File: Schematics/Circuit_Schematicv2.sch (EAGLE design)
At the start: 66 parts, among them Q2 LE33CZ

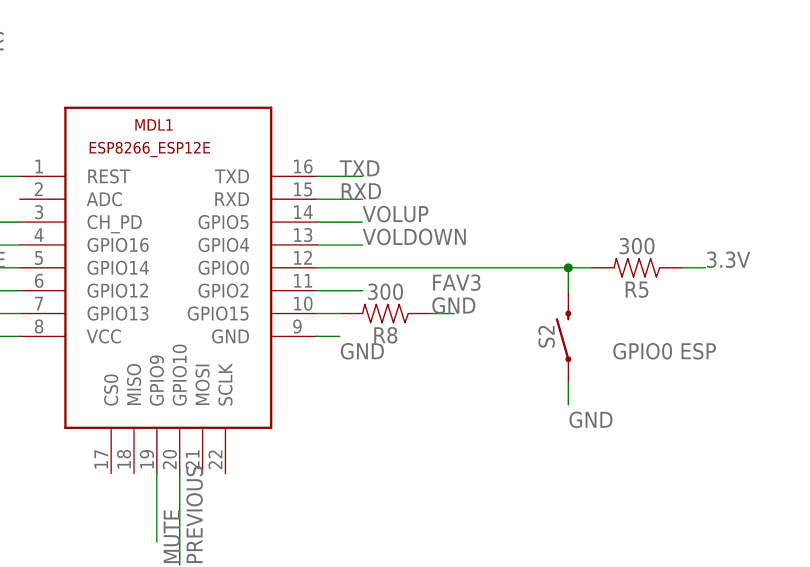
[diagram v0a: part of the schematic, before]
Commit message: Finished the PCB board and schematic
Changes might have to be made based on the testing on Friday the 10th
March
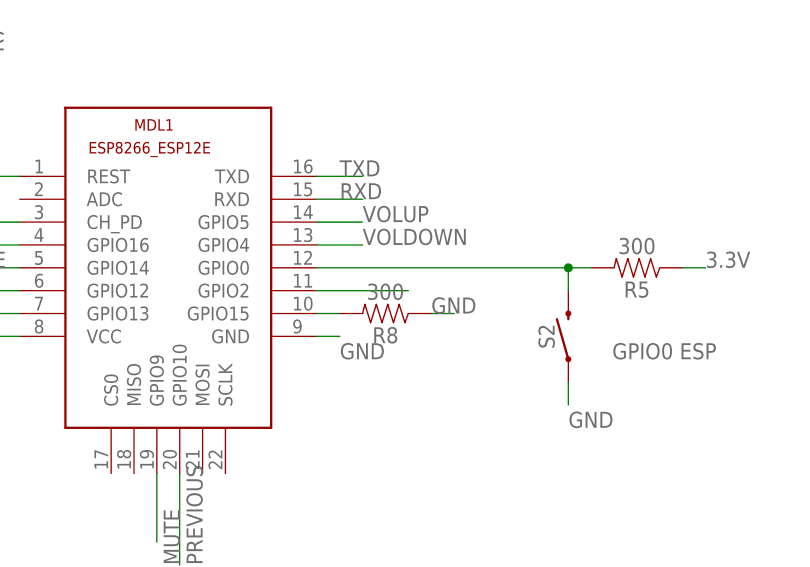
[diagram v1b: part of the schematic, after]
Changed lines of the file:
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@@
 <?xml version="1.0" encoding="utf-8"?>
 <!DOCTYPE eagle SYSTEM "eagle.dtd">
-<eagle version="8.0.0">
+<eagle version="8.0.2">
 <drawing>
 <settings>
@@
 <segment>
 <pinref part="MDL1" gate="G$1" pin="GPIO2"/>
-<wire x1="403.86" y1="50.8" x2="408.94" y2="50.8" width="0.1524" layer="91"/>
-<label x="416.56" y="50.8" size="1.778" layer="95"/>
-</segment>
-</net>
+<wire x1="403.86" y1="50.8" x2="414.02" y2="50.8" width="0.1524" layer="91"/>
+</segment>
+</net>

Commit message: finished the PCB
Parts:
- D1: value (none) -> BLUE; device adafruit:LED -> SparkFun-LED:LED-BLUE1206
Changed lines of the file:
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@@
 <grid distance="0.1" unitdist="inch" unit="inch" style="lines" multiple="1" display="no" altdistance="0.01" altunitdist="inch" altunit="inch"/>
 <layers>
-<layer number="1" name="Top" color="4" fill="1" visible="no" active="no"/>
-<layer number="2" name="Route2" color="1" fill="3" visible="no" active="no"/>
-<layer number="3" name="Route3" color="4" fill="3" visible="no" active="no"/>
-<layer number="4" name="Route4" color="1" fill="4" visible="no" active="no"/>
-<layer number="5" name="Route5" color="4" fill="4" visible="no" active="no"/>
-<layer number="6" name="Route6" color="1" fill="8" visible="no" active="no"/>
-<layer number="7" name="Route7" color="4" fill="8" visible="no" active="no"/>
-<layer number="8" name="Route8" color="1" fill="2" visible="no" active="no"/>
-<layer number="9" name="Route9" color="4" fill="2" visible="no" active="no"/>
-<layer number="10" name="Route10" color="1" fill="7" visible="no" active="no"/>
-<layer number="11" name="Route11" color="4" fill="7" visible="no" active="no"/>
-<layer number="12" name="Route12" color="1" fill="5" visible="no" active="no"/>
-<layer number="13" name="Route13" color="4" fill="5" visible="no" active="no"/>
-<layer number="14" name="Route14" color="1" fill="6" visible="no" active="no"/>
-<layer number="15" name="Route15" color="4" fill="6" visible="no" active="no"/>
-<layer number="16" name="Bottom" color="1" fill="1" visible="no" active="no"/>
-<layer number="17" name="Pads" color="2" fill="1" visible="no" active="no"/>
-<layer number="18" name="Vias" color="2" fill="1" visible="no" active="no"/>
-<layer number="19" name="Unrouted" color="6" fill="1" visible="no" active="no"/>
-<layer number="20" name="Dimension" color="15" fill="1" visible="no" active="no"/>
-<layer number="21" name="tPlace" color="7" fill="1" visible="no" active="no"/>
-<layer number="22" name="bPlace" color="7" fill="1" visible="no" active="no"/>
-<layer number="23" name="tOrigins" color="15" fill="1" visible="no" active="no"/>
-<layer number="24" name="bOrigins" color="15" fill="1" visible="no" active="no"/>
-<layer number="25" name="tNames" color="7" fill="1" visible="no" active="no"/>
-<layer number="26" name="bNames" color="7" fill="1" visible="no" active="no"/>
-<layer number="27" name="tValues" color="7" fill="1" visible="no" active="no"/>
-<layer number="28" name="bValues" color="7" fill="1" visible="no" active="no"/>
+<layer number="1" name="Top" color="4" fill="1" visible="yes" active="no"/>
+<layer number="2" name="Route2" color="1" fill="3" visible="yes" active="no"/>
+<layer number="3" name="Route3" color="4" fill="3" visible="yes" active="no"/>
+<layer number="4" name="Route4" color="1" fill="4" visible="yes" active="no"/>
+<layer number="5" name="Route5" color="4" fill="4" visible="yes" active="no"/>
+<layer number="6" name="Route6" color="1" fill="8" visible="yes" active="no"/>
+<layer number="7" name="Route7" color="4" fill="8" visible="yes" active="no"/>
+<layer number="8" name="Route8" color="1" fill="2" visible="yes" active="no"/>
+<layer number="9" name="Route9" color="4" fill="2" visible="yes" active="no"/>
+<layer number="10" name="Route10" color="1" fill="7" visible="yes" active="no"/>
+<layer number="11" name="Route11" color="4" fill="7" visible="yes" active="no"/>
+<layer number="12" name="Route12" color="1" fill="5" visible="yes" active="no"/>
+<layer number="13" name="Route13" color="4" fill="5" visible="yes" active="no"/>
+<layer number="14" name="Route14" color="1" fill="6" visible="yes" active="no"/>
+<layer number="15" name="Route15" color="4" fill="6" visible="yes" active="no"/>
+<layer number="16" name="Bottom" color="1" fill="1" visible="yes" active="no"/>
+<layer number="17" name="Pads" color="2" fill="1" visible="yes" active="no"/>
+<layer number="18" name="Vias" color="2" fill="1" visible="yes" active="no"/>
+<layer number="19" name="Unrouted" color="6" fill="1" visible="yes" active="no"/>
+<layer number="20" name="Dimension" color="15" fill="1" visible="yes" active="no"/>
+<layer number="21" name="tPlace" color="7" fill="1" visible="yes" active="no"/>
+<layer number="22" name="bPlace" color="7" fill="1" visible="yes" active="no"/>
+<layer number="23" name="tOrigins" color="15" fill="1" visible="yes" active="no"/>
+<layer number="24" name="bOrigins" color="15" fill="1" visible="yes" active="no"/>
+<layer number="25" name="tNames" color="7" fill="1" visible="yes" active="no"/>
+<layer number="26" name="bNames" color="7" fill="1" visible="yes" active="no"/>
+<layer number="27" name="tValues" color="7" fill="1" visible="yes" active="no"/>
+<layer number="28" name="bValues" color="7" fill="1" visible="yes" active="no"/>
 <layer number="29" name="tStop" color="7" fill="3" visible="no" active="no"/>
 <layer number="30" name="bStop" color="7" fill="6" visible="no" active="no"/>
@@
 <layer number="35" name="tGlue" color="7" fill="4" visible="no" active="no"/>
 <layer number="36" name="bGlue" color="7" fill="5" visible="no" active="no"/>
-<layer number="37" name="tTest" color="7" fill="1" visible="no" active="no"/>
-<layer number="38" name="bTest" color="7" fill="1" visible="no" active="no"/>
+<layer number="37" name="tTest" color="7" fill="1" visible="yes" active="no"/>
+<layer number="38" name="bTest" color="7" fill="1" visible="yes" active="no"/>
 <layer number="39" name="tKeepout" color="4" fill="11" visible="no" active="no"/>
 <layer number="40" name="bKeepout" color="1" fill="11" visible="no" active="no"/>
@@
 <layer number="44" name="Drills" color="7" fill="1" visible="no" active="no"/>
 <layer number="45" name="Holes" color="7" fill="1" visible="no" active="no"/>
-<layer number="46" name="Milling" color="3" fill="1" visible="no" active="no"/>
-<layer number="47" name="Measures" color="7" fill="1" visible="no" active="no"/>
-<layer number="48" name="Document" color="7" fill="1" visible="no" active="no"/>
-<layer number="49" name="Reference" color="7" fill="1" visible="no" active="no"/>
-<layer number="50" name="dxf" color="7" fill="1" visible="no" active="no"/>
-<layer number="51" name="tDocu" color="7" fill="1" visible="no" active="no"/>
-<layer number="52" name="bDocu" color="7" fill="1" visible="no" active="no"/>
-<layer number="53" name="tGND_GNDA" color="7" fill="9" visible="no" active="no"/>
-<layer number="54" name="bGND_GNDA" color="1" fill="9" visible="no" active="no"/>
-<layer number="56" name="wert" color="7" fill="1" visible="no" active="no"/>
-<layer number="57" name="tCAD" color="7" fill="1" visible="no" active="no"/>
-<layer number="59" name="tCarbon" color="7" fill="1" visible="no" active="no"/>
-<layer number="60" name="bCarbon" color="7" fill="1" visible="no" active="no"/>
+<layer number="46" name="Milling" color="3" fill="1" visible="yes" active="no"/>
+<layer number="47" name="Measures" color="7" fill="1" visible="yes" active="no"/>
+<layer number="48" name="Document" color="7" fill="1" visible="yes" active="no"/>
+<layer number="49" name="Reference" color="7" fill="1" visible="yes" active="no"/>
+<layer number="50" name="dxf" color="7" fill="1" visible="yes" active="no"/>
+<layer number="51" name="tDocu" color="7" fill="1" visible="yes" active="no"/>
+<layer number="52" name="bDocu" color="7" fill="1" visible="yes" active="no"/>
+<layer number="53" name="tGND_GNDA" color="7" fill="9" visible="yes" active="no"/>
+<layer number="54" name="bGND_GNDA" color="1" fill="9" visible="yes" active="no"/>
+<layer number="56" name="wert" color="7" fill="1" visible="yes" active="no"/>
+<layer number="57" name="tCAD" color="7" fill="1" visible="yes" active="no"/>
+<layer number="59" name="tCarbon" color="7" fill="1" visible="yes" active="no"/>
+<layer number="60" name="bCarbon" color="7" fill="1" visible="yes" active="no"/>
 <layer number="90" name="Modules" color="5" fill="1" visible="yes" active="yes"/>
 <layer number="91" name="Nets" color="2" fill="1" visible="yes" active="yes"/>
@@
 <part name="VR1" library="SparkFun-Resistors" deviceset="TRIMPOT" device="-SMD-3MM-OPEN-1/10W-25%" value="10k"/>
 <part name="MDL1" library="ESP8266-12E" deviceset="ESP8266-12E" device="ESP8266-ESP12E"/>
-<part name="D1" library="adafruit" deviceset="LED" device=""/>
+<part name="D1" library="SparkFun-LED" deviceset="LED-BLUE" device="1206" value="BLUE"/>
 <part name="R1" library="SparkFun-Resistors" deviceset="1OHM" device="-0603-1/10W-1%" value="300"/>
 <part name="U$3" library="MIRO" deviceset="24C64" device=""/>

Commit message: Final changes to make ESP work
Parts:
- added R18: 300, SparkFun-Resistors:1OHM-0603-1/10W-1%
- added S1: GPIO0 ESP, SparkFun-Switches:MOMENTARY-SWITCH-SPST-SMD-6.0X3.5MM
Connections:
- removed net N$8: MDL1.GPIO0, R5.2, S2.2
- net ENABLE: now also R18.2; no longer MDL1.GPIO14
- net GND: now also S1.1
- net MUTE: now also MDL1.GPIO14, R18.1, S1.2; no longer MDL1.GPIO9
- net PREVIOUS: now also MDL1.GPIO0, R5.2, S2.2; no longer MDL1.GPIO10

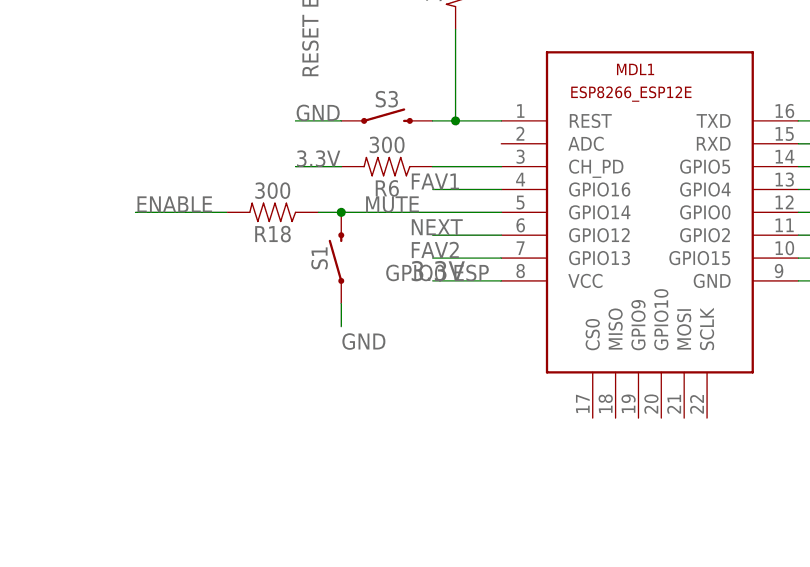
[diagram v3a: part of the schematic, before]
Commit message: Removed unnecessary switch that I put in on GPIO14
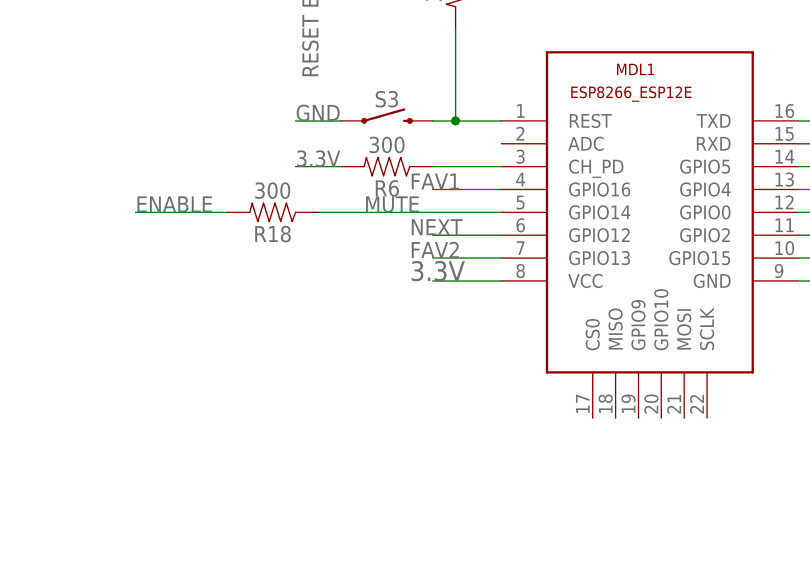
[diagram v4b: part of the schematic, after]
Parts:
- removed S1: GPIO0 ESP, SparkFun-Switches:MOMENTARY-SWITCH-SPST-SMD-6.0X3.5MM
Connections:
- net GND: no longer S1.1
- net MUTE: no longer S1.2
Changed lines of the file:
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@@
 <part name="VR5" library="SparkFun-Resistors" deviceset="TRIMPOT" device="-SMD-3MM-OPEN-1/10W-25%" value="4.7k"/>
 <part name="R18" library="SparkFun-Resistors" deviceset="1OHM" device="-0603-1/10W-1%" value="300"/>
-<part name="S1" library="SparkFun-Switches" deviceset="MOMENTARY-SWITCH-SPST" device="-SMD-6.0X3.5MM" value="GPIO0 ESP"/>
 </parts>
 <sheets>
@@
 <instance part="VR5" gate="R?" x="7.62" y="111.76"/>
 <instance part="R18" gate="G$1" x="345.44" y="53.34" rot="R180"/>
-<instance part="S1" gate="G$1" x="353.06" y="48.26" smashed="yes" rot="R90">
-<attribute name="NAME" x="351.536" y="48.26" size="1.778" layer="95" font="vector" rot="R90" align="bottom-center"/>
-<attribute name="VALUE" x="363.728" y="45.72" size="1.778" layer="96" font="vector" rot="R180" align="top-center"/>
-</instance>
 </instances>
 <busses>
@@
 <pinref part="U$2" gate="G$1" pin="GND"/>
 <wire x1="58.42" y1="101.6" x2="40.64" y2="101.6" width="0.1524" layer="91"/>
-</segment>
-<segment>
-<pinref part="S1" gate="G$1" pin="1"/>
-<wire x1="353.06" y1="43.18" x2="353.06" y2="40.64" width="0.1524" layer="91"/>
-<label x="353.06" y="38.1" size="1.778" layer="95"/>
 </segment>
 </net>
@@
 <segment>
 <pinref part="MDL1" gate="G$1" pin="GPIO14"/>
-<pinref part="S1" gate="G$1" pin="2"/>
-<wire x1="370.84" y1="53.34" x2="353.06" y2="53.34" width="0.1524" layer="91"/>
+<wire x1="370.84" y1="53.34" x2="350.52" y2="53.34" width="0.1524" layer="91"/>
 <pinref part="R18" gate="G$1" pin="1"/>
-<wire x1="353.06" y1="53.34" x2="350.52" y2="53.34" width="0.1524" layer="91"/>
-<junction x="353.06" y="53.34"/>
 <label x="355.6" y="53.34" size="1.778" layer="95"/>
 </segment>

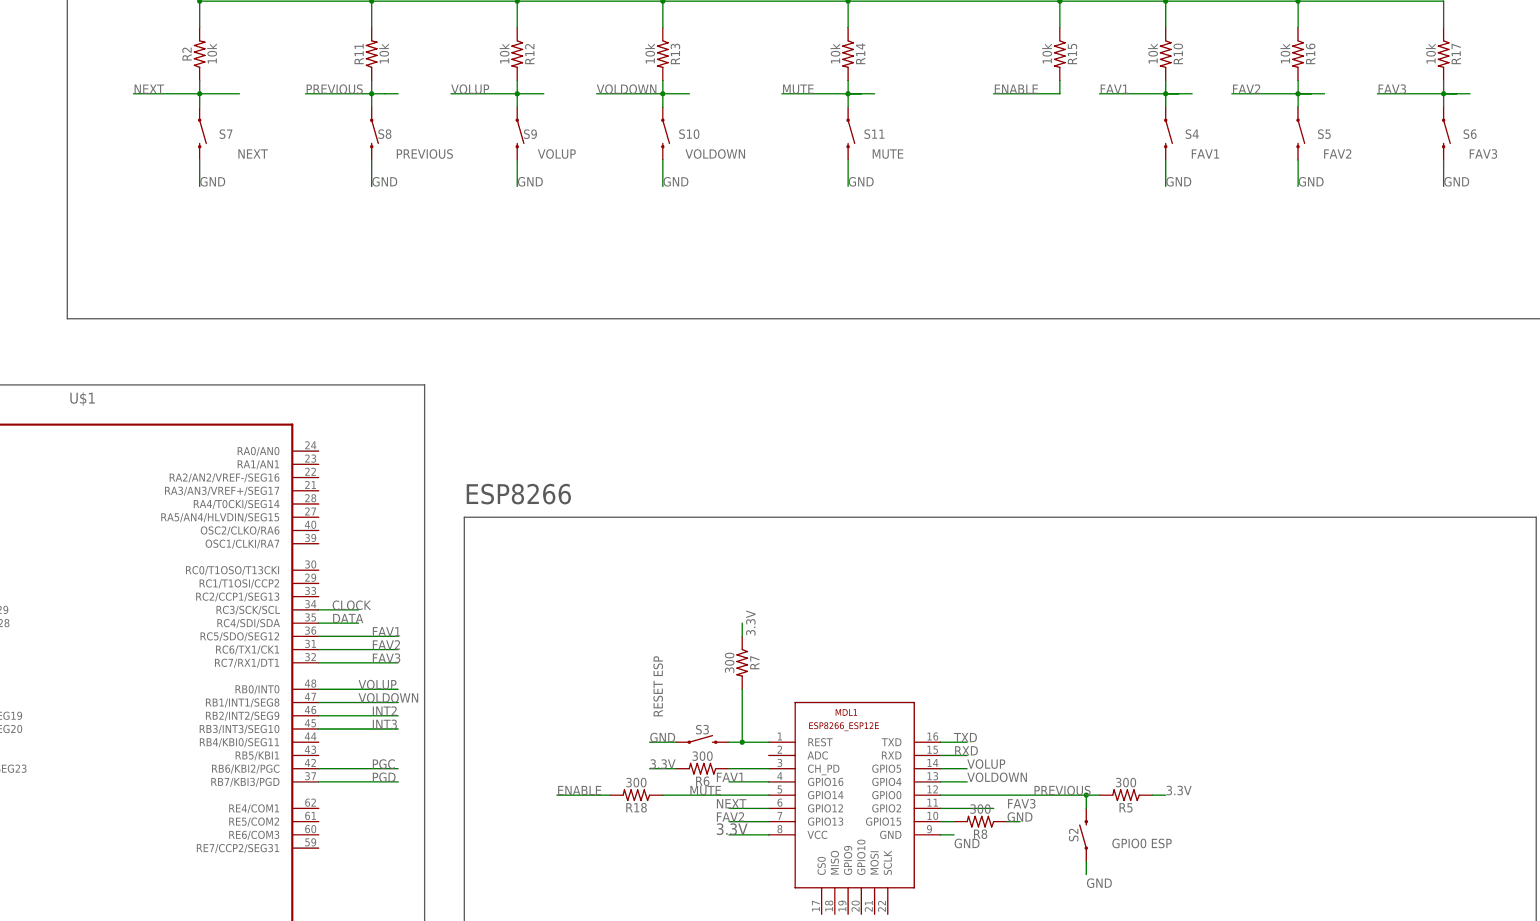
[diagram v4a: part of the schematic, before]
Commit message: Modified circuit to include transistors
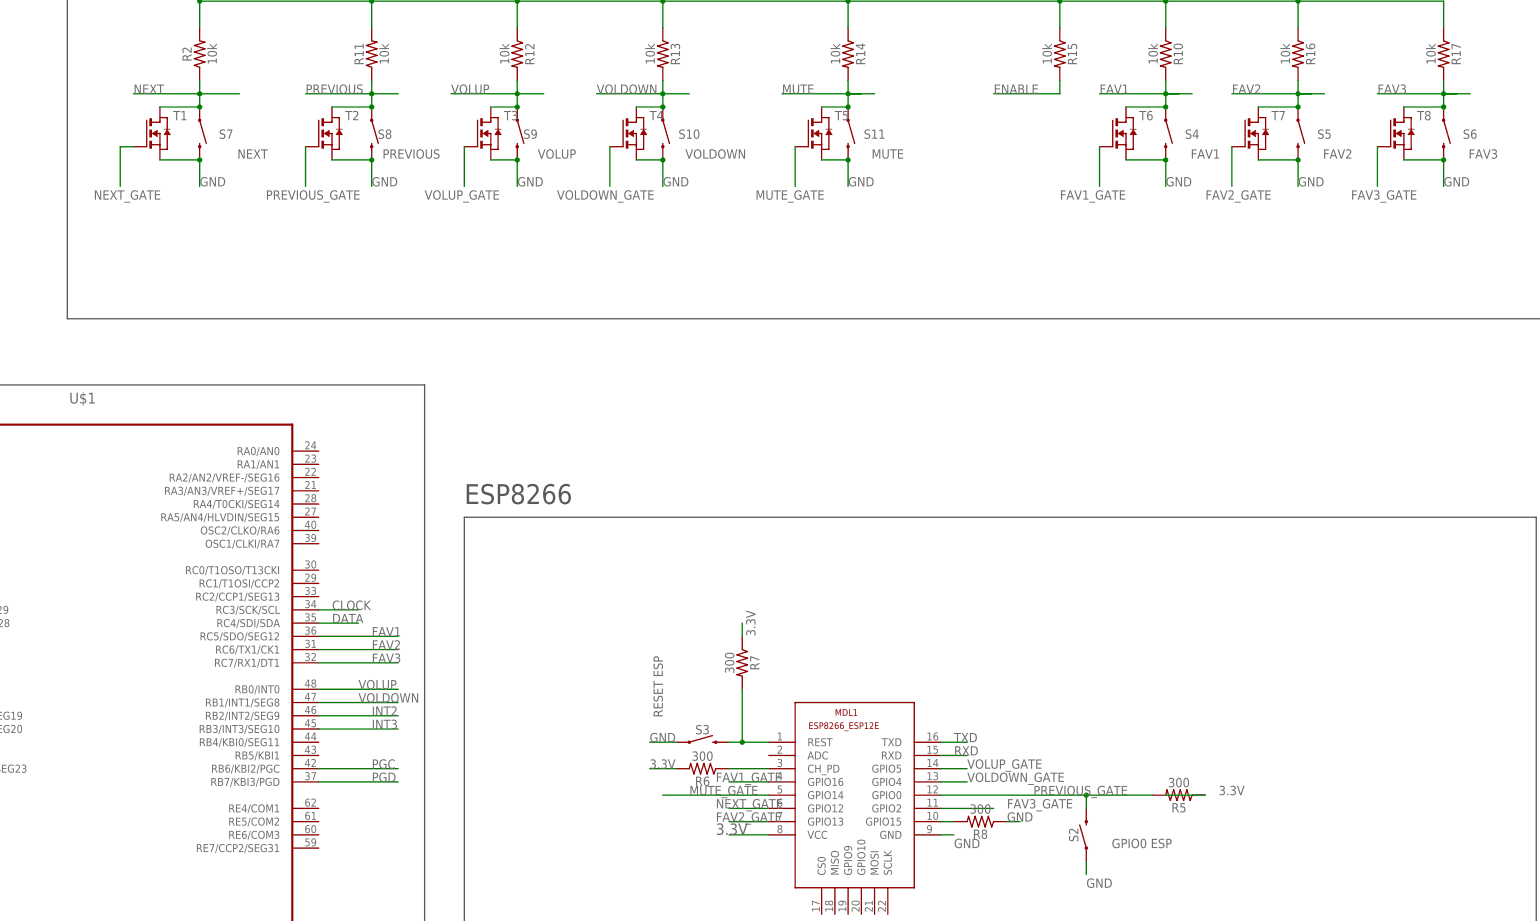
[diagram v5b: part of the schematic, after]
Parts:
- removed R18: 300, SparkFun-Resistors:1OHM-0603-1/10W-1%
- added T1, T2, T3, T4, T5, T6, T7, T8: (no value), zetex:NMOSSOT223
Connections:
- new net FAV1_GATE: MDL1.GPIO16, T6.G
- new net FAV2_GATE: MDL1.GPIO13, T7.G
- new net FAV3_GATE: MDL1.GPIO2, T8.G
- new net MUTE_GATE: MDL1.GPIO14, T5.G
- new net NEXT_GATE: MDL1.GPIO12, T1.G
- new net PREVIOUS_GATE: MDL1.GPIO0, R5.2, S2.2, T2.G
- new net VOLDOWN_GATE: MDL1.GPIO4, T4.G
- new net VOLUP_GATE: MDL1.GPIO5, T3.G
- net ENABLE: no longer R18.2
- net FAV1: now also T6.D; no longer MDL1.GPIO16
- net FAV2: now also T7.D; no longer MDL1.GPIO13
- net FAV3: now also T8.D; no longer MDL1.GPIO2
- net GND: now also T1.S, T2.S, T3.S, T4.S, T5.S, T6.S, T7.S, T8.S
- net MUTE: now also T5.D; no longer MDL1.GPIO14, R18.1
- net NEXT: now also T1.D; no longer MDL1.GPIO12
- net PREVIOUS: now also T2.D; no longer MDL1.GPIO0, R5.2, S2.2
- net VOLDOWN: now also T4.D; no longer MDL1.GPIO4
- net VOLUP: now also T3.D; no longer MDL1.GPIO5
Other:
- moved on the sheet: R5
